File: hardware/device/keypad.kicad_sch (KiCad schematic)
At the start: 50 parts, among them SW1 TRIG1, SW10 TRIG10, SW11 TRIG11, SW12 TRIG12, SW13 TRIG13, SW14 TRIG14, SW15 TRIG15, SW16 TRIG16, SW17 WHEEL_BTN, SW18 HELP, SW19 LEFT_BTN, SW2 TRIG2, SW20 RIGHT_BTN, SW3 TRIG3, SW4 TRIG4, SW5 TRIG5, SW6 TRIG6, SW7 TRIG7, SW8 TRIG8, SW9 TRIG9, U25 TCA8418RTWR

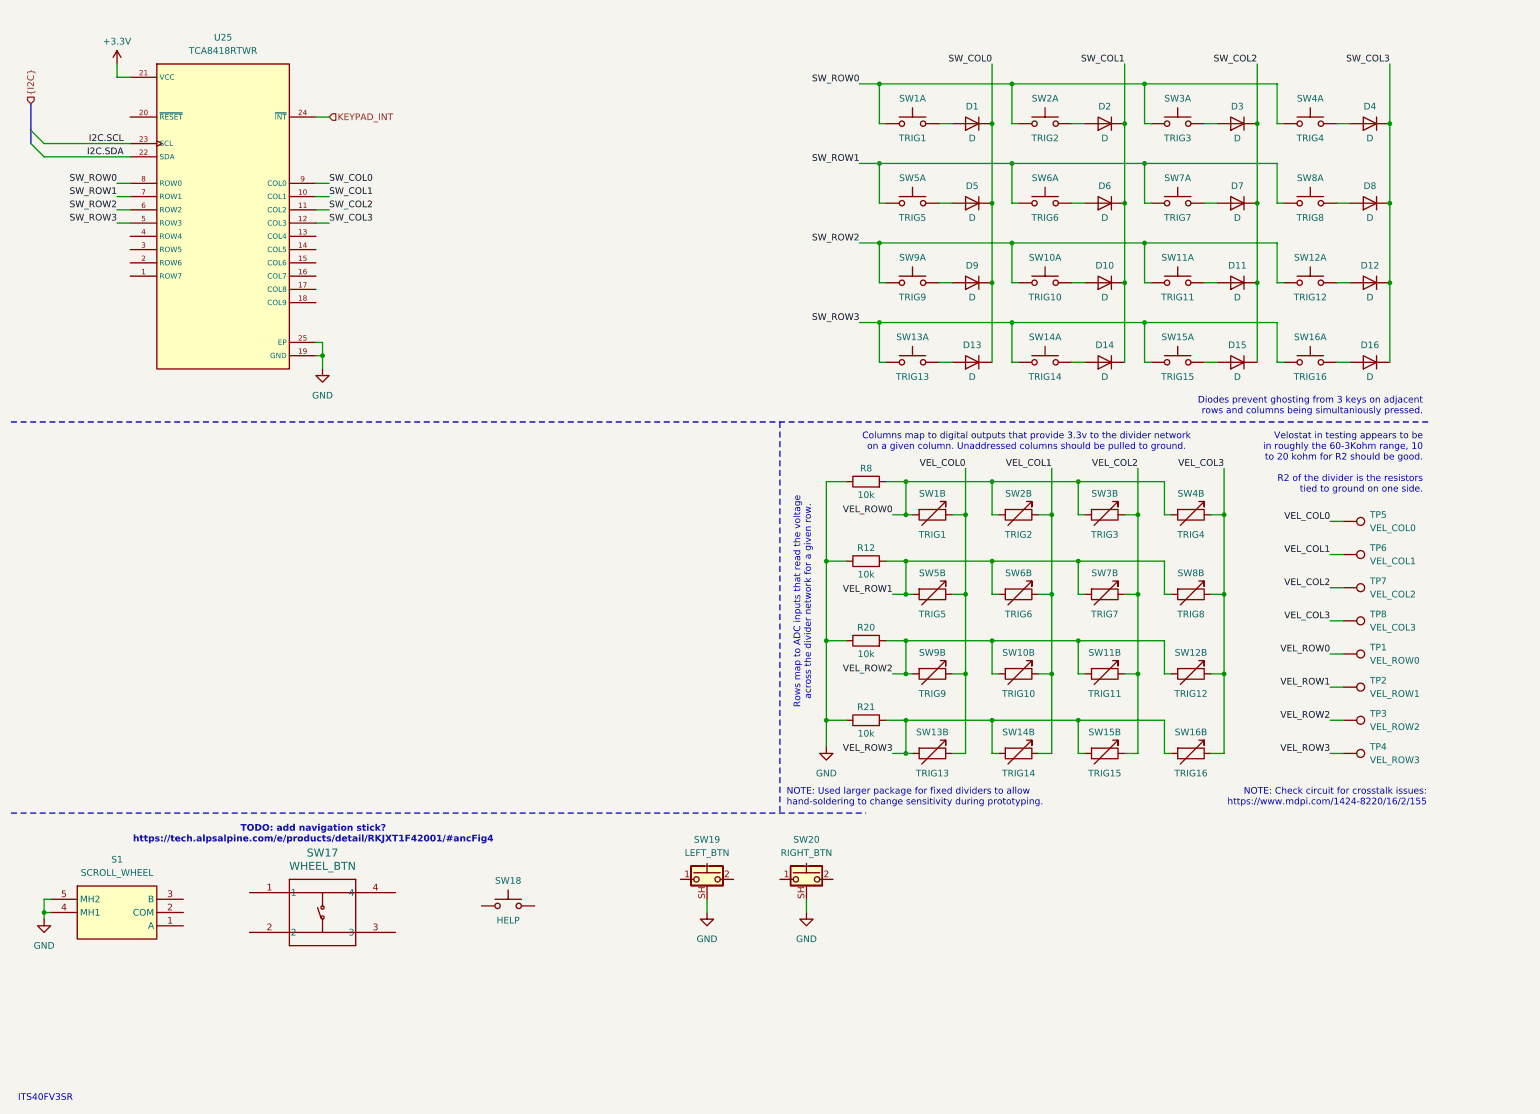
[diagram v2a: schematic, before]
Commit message: feat: update board layout to include velocity matrix
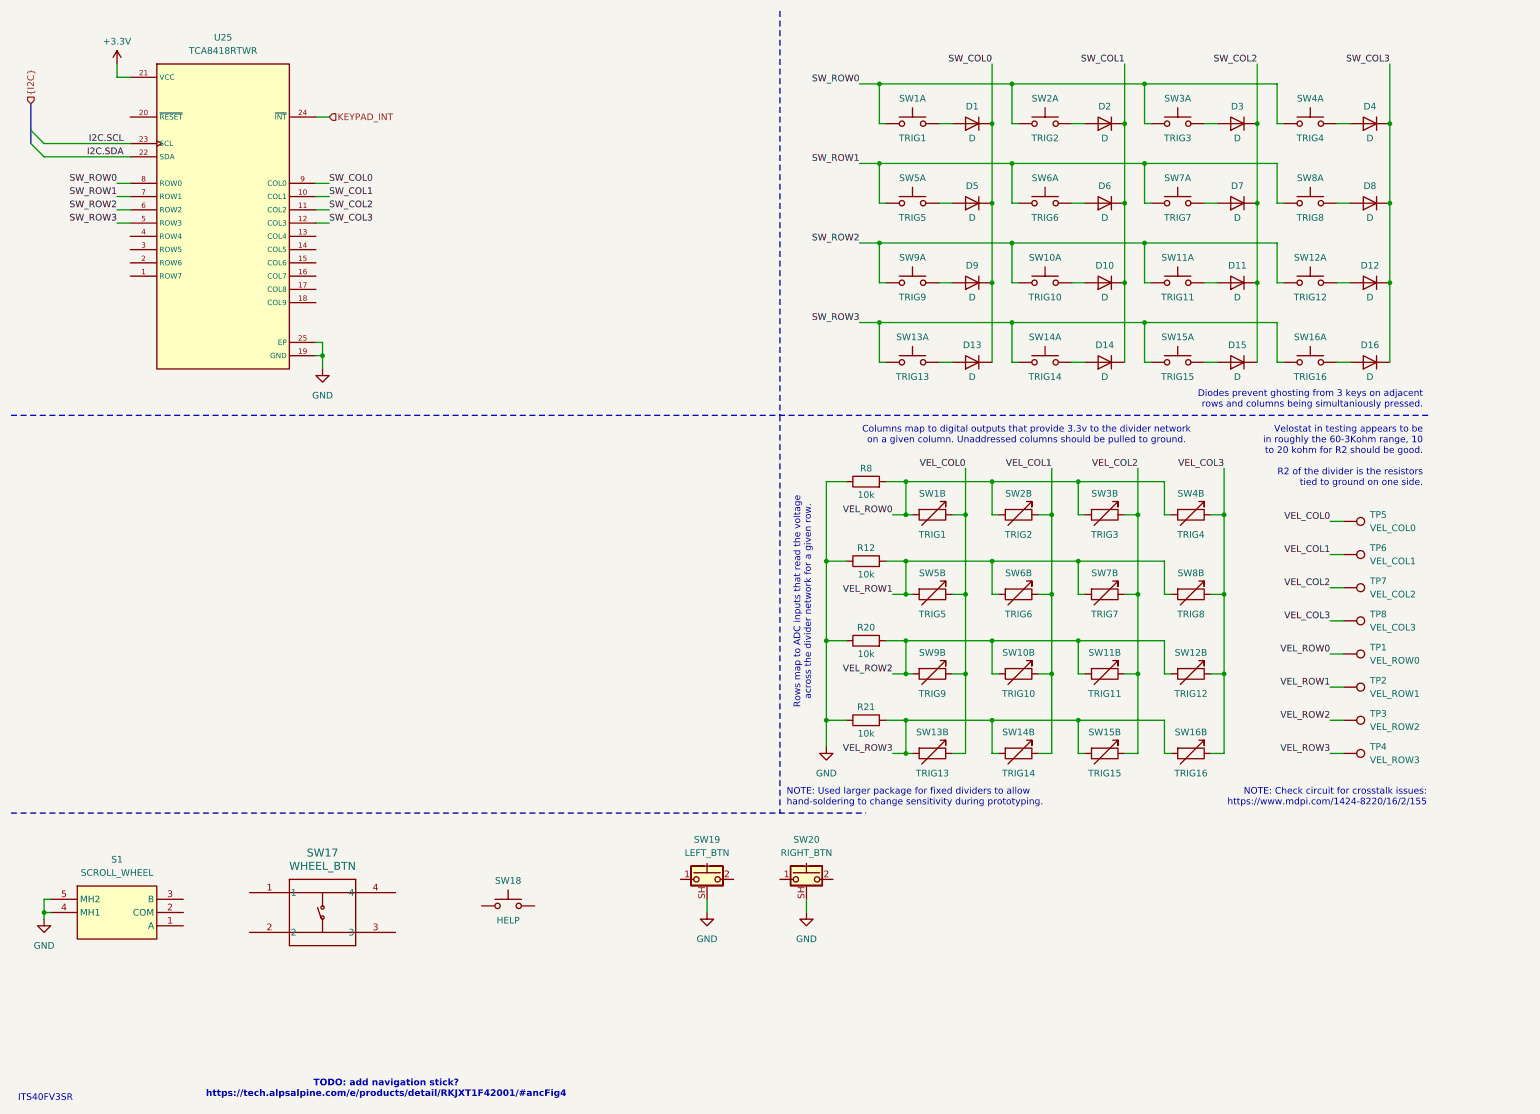
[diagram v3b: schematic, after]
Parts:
- SW1, SW10, SW11, SW12, SW13, SW14, SW15, SW2, SW3, SW4, SW5, SW6, SW7, SW8, SW9: footprint pocket_synth:SW_Hotswap_Kailh_Choc_V1V2_Plated_1.00u -> pocket_synth:SW_Hotswap_Kailh_Choc_V1_1.00u_Pressure
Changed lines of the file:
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@@
 	(text "Velostat in testing appears to be \nin roughly the 60-3Kohm range, 10\nto 20 kohm for R2 should be good.\n\nR2 of the divider is the resistors\ntied to ground on one side.\n"
 		(exclude_from_sim no)
-		(at 283.21 93.472 0)
+		(at 283.21 92.202 0)
 		(effects
 			(font
@@
 	(text "TODO: add navigation stick?\nhttps://tech.alpsalpine.com/e/products/detail/RKJXT1F42001/#ancFig4"
 		(exclude_from_sim no)
-		(at 70.612 170.434 0)
+		(at 84.582 219.202 0)
 		(effects
 			(font
@@
 	(text "Diodes prevent ghosting from 3 keys on adjacent\nrows and columns being simultaniously pressed."
 		(exclude_from_sim no)
-		(at 283.21 90.17 0)
+		(at 283.21 88.9 0)
 		(effects
 			(font
@@
 	(text "Columns map to digital outputs that provide 3.3v to the divider network\non a given column. Unaddressed columns should be pulled to ground."
 		(exclude_from_sim no)
-		(at 207.264 93.472 0)
+		(at 207.264 92.202 0)
 		(effects
 			(font
@@
 	(polyline
 		(pts
-			(xy 160.02 91.44) (xy 160.02 166.37)
+			(xy 160.02 90.17) (xy 160.02 166.37)
 		)
 		(stroke
@@
 		)
 	)
+	(polyline
+		(pts
+			(xy 160.02 12.7) (xy 160.02 90.17)
+		)
+		(stroke
+			(width 0.2032)
+			(type dash)
+		)
+	)
 	(wire
 		(pts
@@
 	(polyline
 		(pts
-			(xy 12.7 91.44) (xy 284.48 91.44)
+			(xy 12.7 90.17) (xy 284.48 90.17)
 		)
 		(stroke
@@
 			)
 		)
-		(property "Footprint" "pocket_synth:SW_Hotswap_Kailh_Choc_V1V2_Plated_1.00u"
+		(property "Footprint" "pocket_synth:SW_Hotswap_Kailh_Choc_V1_1.00u_Pressure"
 			(at 210.8835 44.5135 0)
 			(effects
@@
 			)
 		)
-		(property "Footprint" "pocket_synth:SW_Hotswap_Kailh_Choc_V1V2_Plated_1.00u"
+		(property "Footprint" "pocket_synth:SW_Hotswap_Kailh_Choc_V1_1.00u_Pressure"
 			(at 205.8035 119.4435 0)
 			(effects
@@
 			)
 		)
-		(property "Footprint" "pocket_synth:SW_Hotswap_Kailh_Choc_V1V2_Plated_1.00u"
+		(property "Footprint" "pocket_synth:SW_Hotswap_Kailh_Choc_V1_1.00u_Pressure"
 			(at 185.4835 74.9935 0)
 			(effects
@@
 			)
 		)
-		(property "Footprint" "pocket_synth:SW_Hotswap_Kailh_Choc_V1V2_Plated_1.00u"
+		(property "Footprint" "pocket_synth:SW_Hotswap_Kailh_Choc_V1_1.00u_Pressure"
 			(at 189.2935 149.9235 0)
 			(effects
@@
 			)
 		)
-		(property "Footprint" "pocket_synth:SW_Hotswap_Kailh_Choc_V1V2_Plated_1.00u"
+		(property "Footprint" "pocket_synth:SW_Hotswap_Kailh_Choc_V1_1.00u_Pressure"
 			(at 236.2835 59.7535 0)
 			(effects
@@
 			)
 		)
-		(property "Footprint" "pocket_synth:SW_Hotswap_Kailh_Choc_V1V2_Plated_1.00u"
+		(property "Footprint" "pocket_synth:SW_Hotswap_Kailh_Choc_V1_1.00u_Pressure"
 			(at 222.3135 134.6835 0)
 			(effects
@@
 			)
 		)
-		(property "Footprint" "pocket_synth:SW_Hotswap_Kailh_Choc_V1V2_Plated_1.00u"
+		(property "Footprint" "pocket_synth:SW_Hotswap_Kailh_Choc_V1_1.00u_Pressure"
 			(at 261.6835 29.2735 0)
 			(effects
@@
 			)
 		)
-		(property "Footprint" "pocket_synth:SW_Hotswap_Kailh_Choc_V1V2_Plated_1.00u"
+		(property "Footprint" "pocket_synth:SW_Hotswap_Kailh_Choc_V1_1.00u_Pressure"
 			(at 238.8235 104.2035 0)
 			(effects
@@
 			)
 		)
-		(property "Footprint" "pocket_synth:SW_Hotswap_Kailh_Choc_V1V2_Plated_1.00u"
+		(property "Footprint" "pocket_synth:SW_Hotswap_Kailh_Choc_V1_1.00u_Pressure"
 			(at 236.2835 74.9935 0)
 			(effects
@@
 			)
 		)
-		(property "Footprint" "pocket_synth:SW_Hotswap_Kailh_Choc_V1V2_Plated_1.00u"
+		(property "Footprint" "pocket_synth:SW_Hotswap_Kailh_Choc_V1_1.00u_Pressure"
 			(at 222.3135 149.9235 0)
 			(effects
@@
 			)
 		)
-		(property "Footprint" "pocket_synth:SW_Hotswap_Kailh_Choc_V1V2_Plated_1.00u"
+		(property "Footprint" "pocket_synth:SW_Hotswap_Kailh_Choc_V1_1.00u_Pressure"
 			(at 185.4835 29.2735 0)
 			(effects
@@
 			)
 		)
-		(property "Footprint" "pocket_synth:SW_Hotswap_Kailh_Choc_V1V2_Plated_1.00u"
+		(property "Footprint" "pocket_synth:SW_Hotswap_Kailh_Choc_V1_1.00u_Pressure"
 			(at 189.2935 104.2035 0)
 			(effects
@@
 			)
 		)
-		(property "Footprint" "pocket_synth:SW_Hotswap_Kailh_Choc_V1V2_Plated_1.00u"
+		(property "Footprint" "pocket_synth:SW_Hotswap_Kailh_Choc_V1_1.00u_Pressure"
 			(at 261.6835 44.5135 0)
 			(effects
@@
 			)
 		)
-		(property "Footprint" "pocket_synth:SW_Hotswap_Kailh_Choc_V1V2_Plated_1.00u"
+		(property "Footprint" "pocket_synth:SW_Hotswap_Kailh_Choc_V1_1.00u_Pressure"
 			(at 238.8235 119.4435 0)
 			(effects
@@
 			)
 		)
-		(property "Footprint" "pocket_synth:SW_Hotswap_Kailh_Choc_V1V2_Plated_1.00u"
+		(property "Footprint" "pocket_synth:SW_Hotswap_Kailh_Choc_V1_1.00u_Pressure"
 			(at 261.6835 59.7535 0)
 			(effects
@@
 			)
 		)
-		(property "Footprint" "pocket_synth:SW_Hotswap_Kailh_Choc_V1V2_Plated_1.00u"
+		(property "Footprint" "pocket_synth:SW_Hotswap_Kailh_Choc_V1_1.00u_Pressure"
 			(at 238.8235 134.6835 0)
 			(effects
@@
 			)
 		)
-		(property "Footprint" "pocket_synth:SW_Hotswap_Kailh_Choc_V1V2_Plated_1.00u"
+		(property "Footprint" "pocket_synth:SW_Hotswap_Kailh_Choc_V1_1.00u_Pressure"
 			(at 210.8835 74.9935 0)
 			(effects
@@
 			)
 		)
-		(property "Footprint" "pocket_synth:SW_Hotswap_Kailh_Choc_V1V2_Plated_1.00u"
+		(property "Footprint" "pocket_synth:SW_Hotswap_Kailh_Choc_V1_1.00u_Pressure"
 			(at 205.8035 149.9235 0)
 			(effects
@@
 			)
 		)
-		(property "Footprint" "pocket_synth:SW_Hotswap_Kailh_Choc_V1V2_Plated_1.00u"
+		(property "Footprint" "pocket_synth:SW_Hotswap_Kailh_Choc_V1_1.00u_Pressure"
 			(at 185.4835 59.7535 0)
 			(effects
@@
 			)
 		)
-		(property "Footprint" "pocket_synth:SW_Hotswap_Kailh_Choc_V1V2_Plated_1.00u"
+		(property "Footprint" "pocket_synth:SW_Hotswap_Kailh_Choc_V1_1.00u_Pressure"
 			(at 189.2935 134.6835 0)
 			(effects
@@
 			)
 		)
-		(property "Footprint" "pocket_synth:SW_Hotswap_Kailh_Choc_V1V2_Plated_1.00u"
+		(property "Footprint" "pocket_synth:SW_Hotswap_Kailh_Choc_V1_1.00u_Pressure"
 			(at 185.4835 44.5135 0)
 			(effects
@@
 			)
 		)
-		(property "Footprint" "pocket_synth:SW_Hotswap_Kailh_Choc_V1V2_Plated_1.00u"
+		(property "Footprint" "pocket_synth:SW_Hotswap_Kailh_Choc_V1_1.00u_Pressure"
 			(at 189.2935 119.4435 0)
 			(effects
@@
 			)
 		)
-		(property "Footprint" "pocket_synth:SW_Hotswap_Kailh_Choc_V1V2_Plated_1.00u"
+		(property "Footprint" "pocket_synth:SW_Hotswap_Kailh_Choc_V1_1.00u_Pressure"
 			(at 210.8835 59.7535 0)
 			(effects
@@
 			)
 		)
-		(property "Footprint" "pocket_synth:SW_Hotswap_Kailh_Choc_V1V2_Plated_1.00u"
+		(property "Footprint" "pocket_synth:SW_Hotswap_Kailh_Choc_V1_1.00u_Pressure"
 			(at 205.8035 134.6835 0)
 			(effects
@@
 			)
 		)
-		(property "Footprint" "pocket_synth:SW_Hotswap_Kailh_Choc_V1V2_Plated_1.00u"
+		(property "Footprint" "pocket_synth:SW_Hotswap_Kailh_Choc_V1_1.00u_Pressure"
 			(at 210.8835 29.2735 0)
 			(effects
@@
 			)
 		)
-		(property "Footprint" "pocket_synth:SW_Hotswap_Kailh_Choc_V1V2_Plated_1.00u"
+		(property "Footprint" "pocket_synth:SW_Hotswap_Kailh_Choc_V1_1.00u_Pressure"
 			(at 205.8035 104.2035 0)
 			(effects
@@
 			)
 		)
-		(property "Footprint" "pocket_synth:SW_Hotswap_Kailh_Choc_V1V2_Plated_1.00u"
+		(property "Footprint" "pocket_synth:SW_Hotswap_Kailh_Choc_V1_1.00u_Pressure"
 			(at 236.2835 29.2735 0)
 			(effects
@@
 			)
 		)
-		(property "Footprint" "pocket_synth:SW_Hotswap_Kailh_Choc_V1V2_Plated_1.00u"
+		(property "Footprint" "pocket_synth:SW_Hotswap_Kailh_Choc_V1_1.00u_Pressure"
 			(at 222.3135 104.2035 0)
 			(effects
@@
 			)
 		)
-		(property "Footprint" "pocket_synth:SW_Hotswap_Kailh_Choc_V1V2_Plated_1.00u"
+		(property "Footprint" "pocket_synth:SW_Hotswap_Kailh_Choc_V1_1.00u_Pressure"
 			(at 236.2835 44.5135 0)
 			(effects
@@
 			)
 		)
-		(property "Footprint" "pocket_synth:SW_Hotswap_Kailh_Choc_V1V2_Plated_1.00u"
+		(property "Footprint" "pocket_synth:SW_Hotswap_Kailh_Choc_V1_1.00u_Pressure"
 			(at 222.3135 119.4435 0)
 			(effects

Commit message: feat: add anti-ghosting resistors to resistive matrix
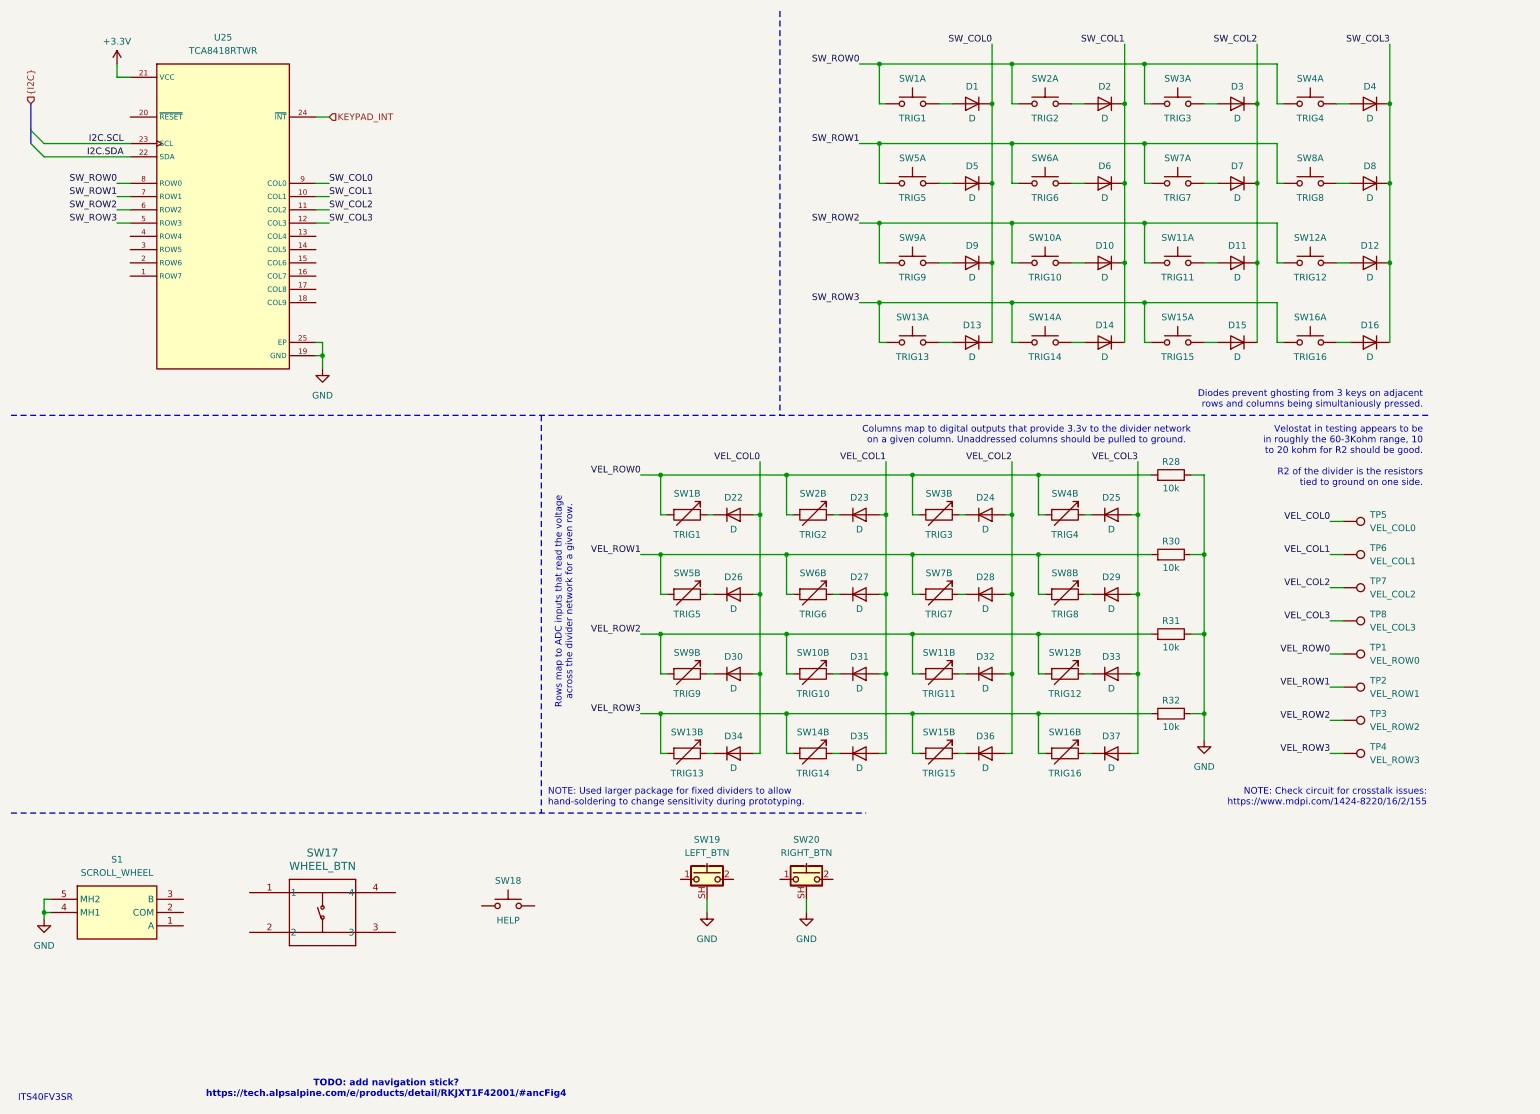
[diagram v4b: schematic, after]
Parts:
- removed R12, R20, R21, R8: 10k, Resistor_SMD:R_0805_2012Metric, symbol Device:R
- added D22, D23, D24, D25, D26, D27, D28, D29, D30, D31, D32, D33, D34, D35, D36, D37: D, Diode_SMD:D_0603_1608Metric_Pad1.05x0.95mm_HandSolder, symbol Device:D
- added R28, R30, R31, R32: 10k, Resistor_SMD:R_0805_2012Metric_Pad1.20x1.40mm_HandSolder, symbol Device:R
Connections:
- net GND: now also R28.1, R30.1, R31.1, R32.1
- net VEL_COL0: now also D22.2 (A), D26.2 (A), D30.2 (A), D34.2 (A); no longer SW1.4, SW13.4, SW5.4, SW9.4
- net VEL_COL1: now also D23.2 (A), D27.2 (A), D31.2 (A), D35.2 (A); no longer SW10.4, SW14.4, SW2.4, SW6.4
- net VEL_COL2: now also D24.2 (A), D28.2 (A), D32.2 (A), D36.2 (A); no longer SW11.4, SW15.4, SW3.4, SW7.4
- net VEL_COL3: now also D25.2 (A), D29.2 (A), D33.2 (A), D37.2 (A); no longer SW12.4, SW16.4, SW4.4, SW8.4
- net VEL_ROW0: now also R28.2
- net VEL_ROW1: now also R30.2
- net VEL_ROW2: now also R31.2
- net VEL_ROW3: now also R32.2
- new net: D29.1 (K), SW8.4
- new net: D37.1 (K), SW16.4
- new net: D26.1 (K), SW5.4
- new net: D31.1 (K), SW10.4
- new net: D23.1 (K), SW2.4
- new net: D33.1 (K), SW12.4
- new net: D32.1 (K), SW11.4
- new net: D22.1 (K), SW1.4
- new net: D24.1 (K), SW3.4
- new net: D30.1 (K), SW9.4
- new net: D25.1 (K), SW4.4
- new net: D34.1 (K), SW13.4
- new net: D35.1 (K), SW14.4
- new net: D28.1 (K), SW7.4
- new net: D36.1 (K), SW15.4
- new net: D27.1 (K), SW6.4
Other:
- moved on the sheet: D1, D10, D11, D12, D13, D14, D15, D16, D2, D3, D4, D5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
